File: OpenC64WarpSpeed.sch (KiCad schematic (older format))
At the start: 15 parts, among them P1 C64-Exp-Port, SW1 SW_C64_C128, SW2 SW_Push, U1 74LS109, U2 27128

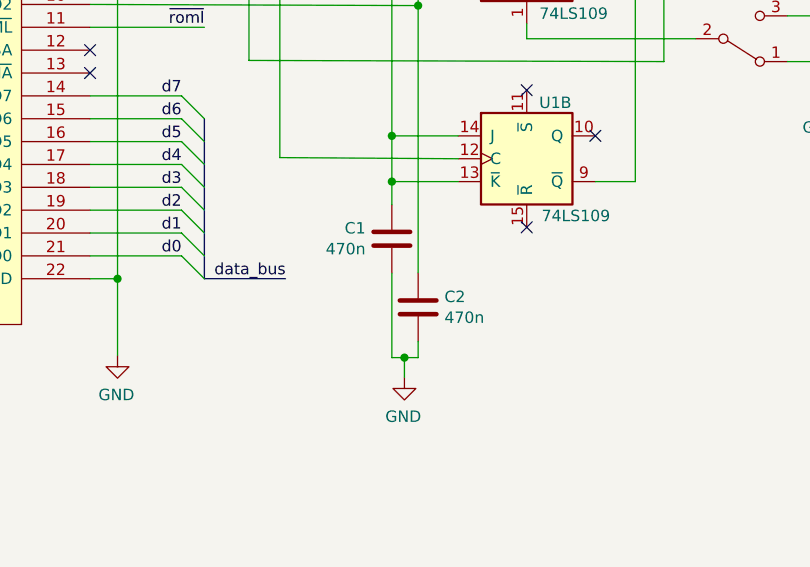
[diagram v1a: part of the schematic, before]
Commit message: Fix capacitor value: 470nF -> 47pF - Thanks @svenpetersen1965
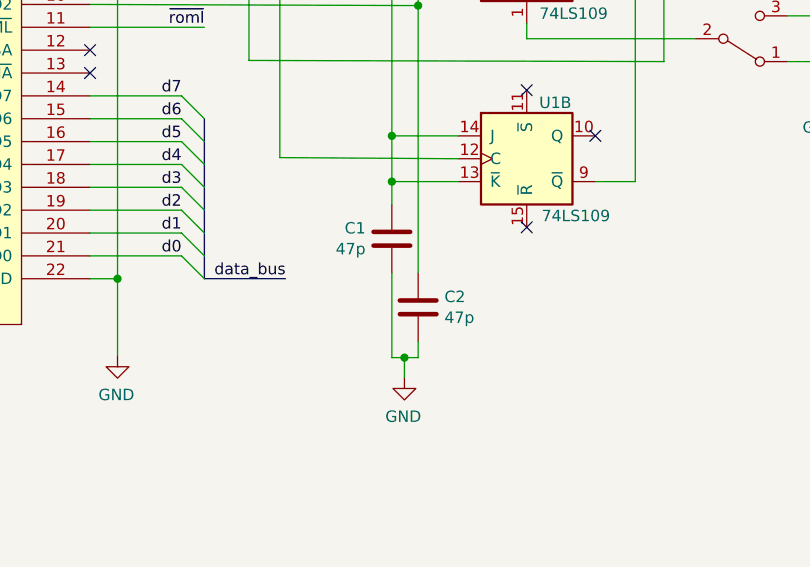
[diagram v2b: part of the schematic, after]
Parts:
- C1, C2: value 470n -> 47p
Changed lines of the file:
@@
 Sheet 1 1
 Title "OpenC64WarpSpeed"
-Date "2020-03-27"
+Date "2020-10-25"
 Rev "1orig"
 Comp "SukkoPera"
@@
 P 5165 4800
 F 0 "C1" H 5050 4846 50  0000 R CNN
-F 1 "470n" H 5050 4755 50  0000 R CNN
+F 1 "47p" H 5050 4755 50  0000 R CNN
 F 2 "OpenC64WarpSpeed:C_Disc_D7.5mm_W2.50mm_P7.50mm" H 5203 4650 50  0001 C CNN
 F 3 "~" H 5165 4800 50  0001 C CNN
@@
 P 5280 5100
 F 0 "C2" H 5395 5146 50  0000 L CNN
-F 1 "470n" H 5395 5055 50  0000 L CNN
+F 1 "47p" H 5395 5055 50  0000 L CNN
 F 2 "OpenC64WarpSpeed:C_Disc_D7.5mm_W2.50mm_P7.50mm" H 5318 4950 50  0001 C CNN
 F 3 "~" H 5280 5100 50  0001 C CNN
